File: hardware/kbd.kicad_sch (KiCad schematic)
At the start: 75 parts, among them J1 Conn_01x12_MountingPin, J2 Conn_01x12_MountingPin, SW00 SW_Push, SW01 SW_Push, SW02 SW_Push, SW03 SW_Push, SW04 SW_Push, SW05 SW_Push, SW10 SW_Push, SW11 SW_Push, SW12 SW_Push, SW13 SW_Push, SW14 SW_Push, SW15 SW_Push, SW20 SW_Push, SW21 SW_Push, SW22 SW_Push, SW23 SW_Push, SW24 SW_Push, SW25 SW_Push, SW30 SW_Push, SW31 SW_Push, SW32 SW_Push, SW33 SW_Push, SW34 SW_Push, SW35 SW_Push, SW36 SW_Push, SW37 SW_Push, U1 CH582, U2 74HC165, U4 74HC165

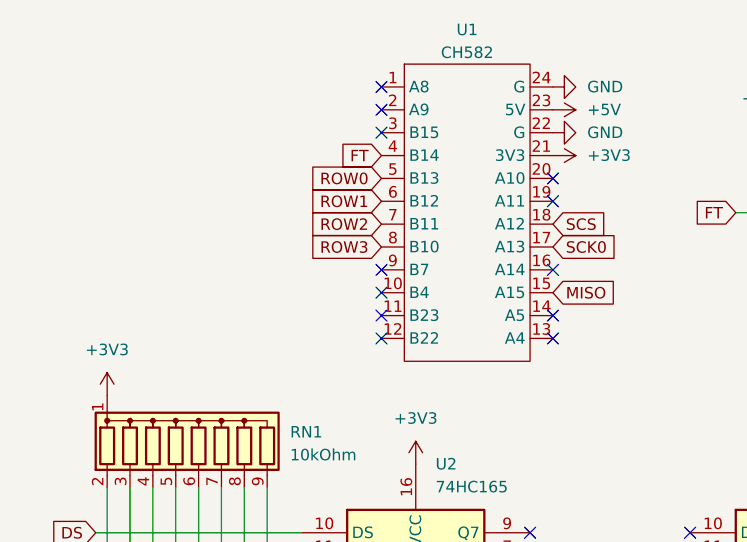
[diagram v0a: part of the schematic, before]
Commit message: Fixed row2 and row3 pin connections and added gerber files
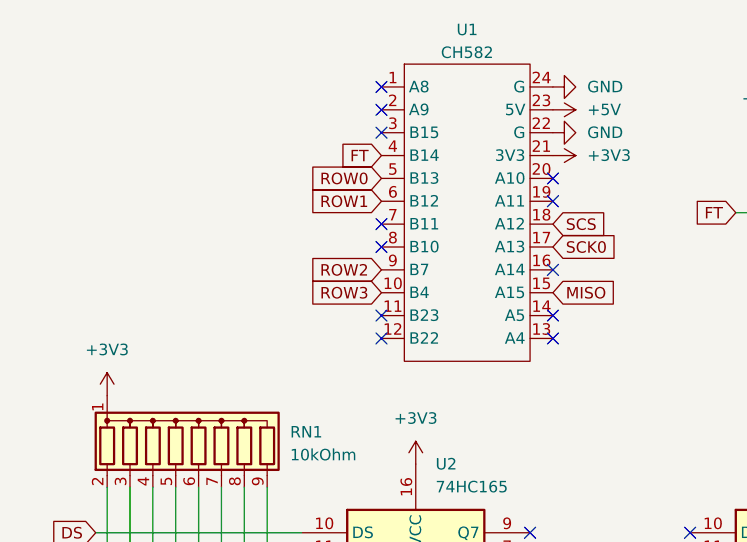
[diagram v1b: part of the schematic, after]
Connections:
- net ROW2: now also U1.9 (B7); no longer U1.7 (B11)
- net ROW3: now also U1.10 (B4); no longer U1.8 (B10)

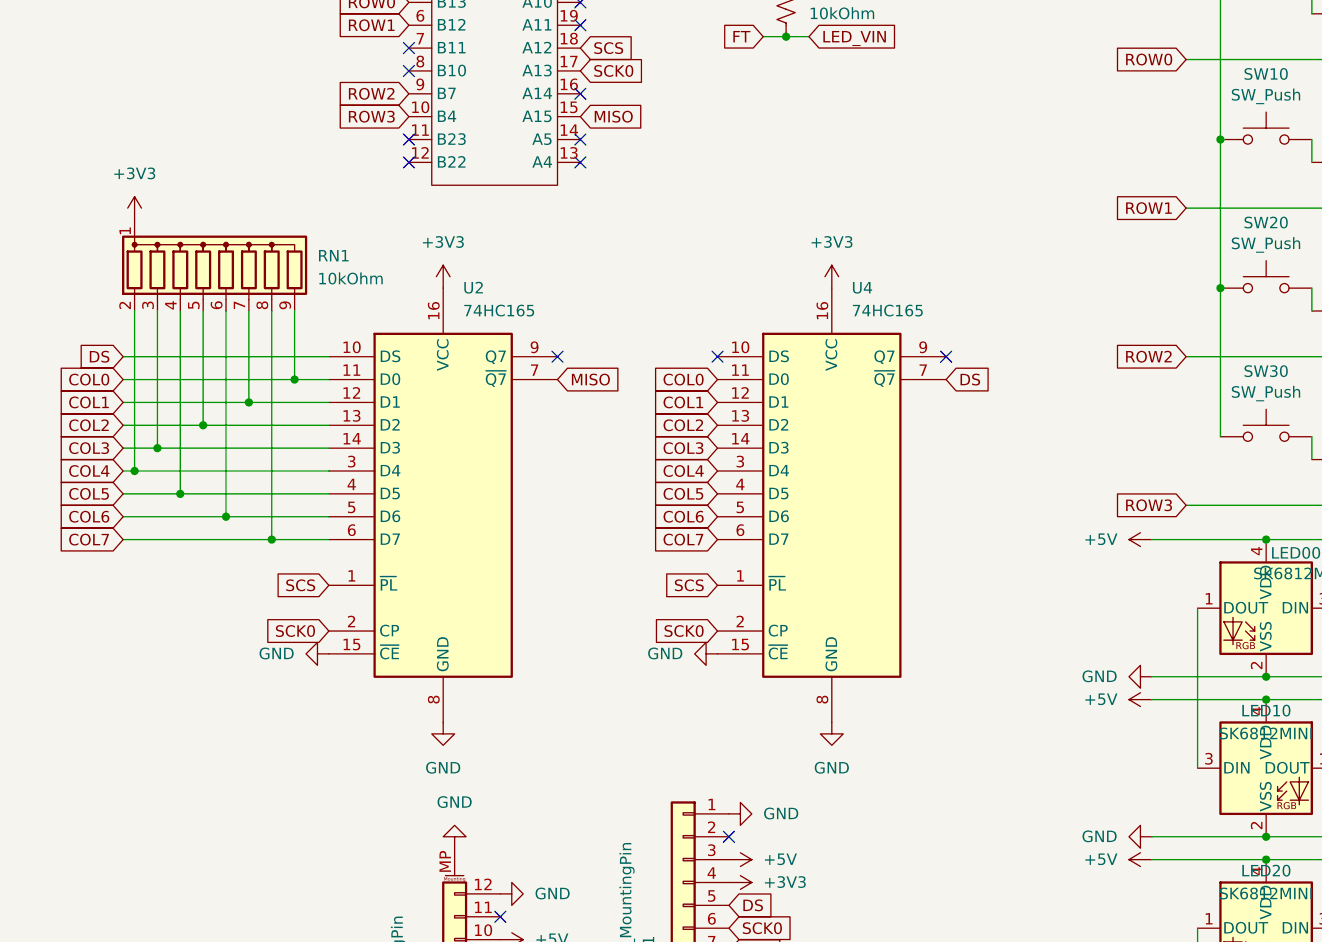
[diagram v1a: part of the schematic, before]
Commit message: Replaced SIP resistor with 0602x8
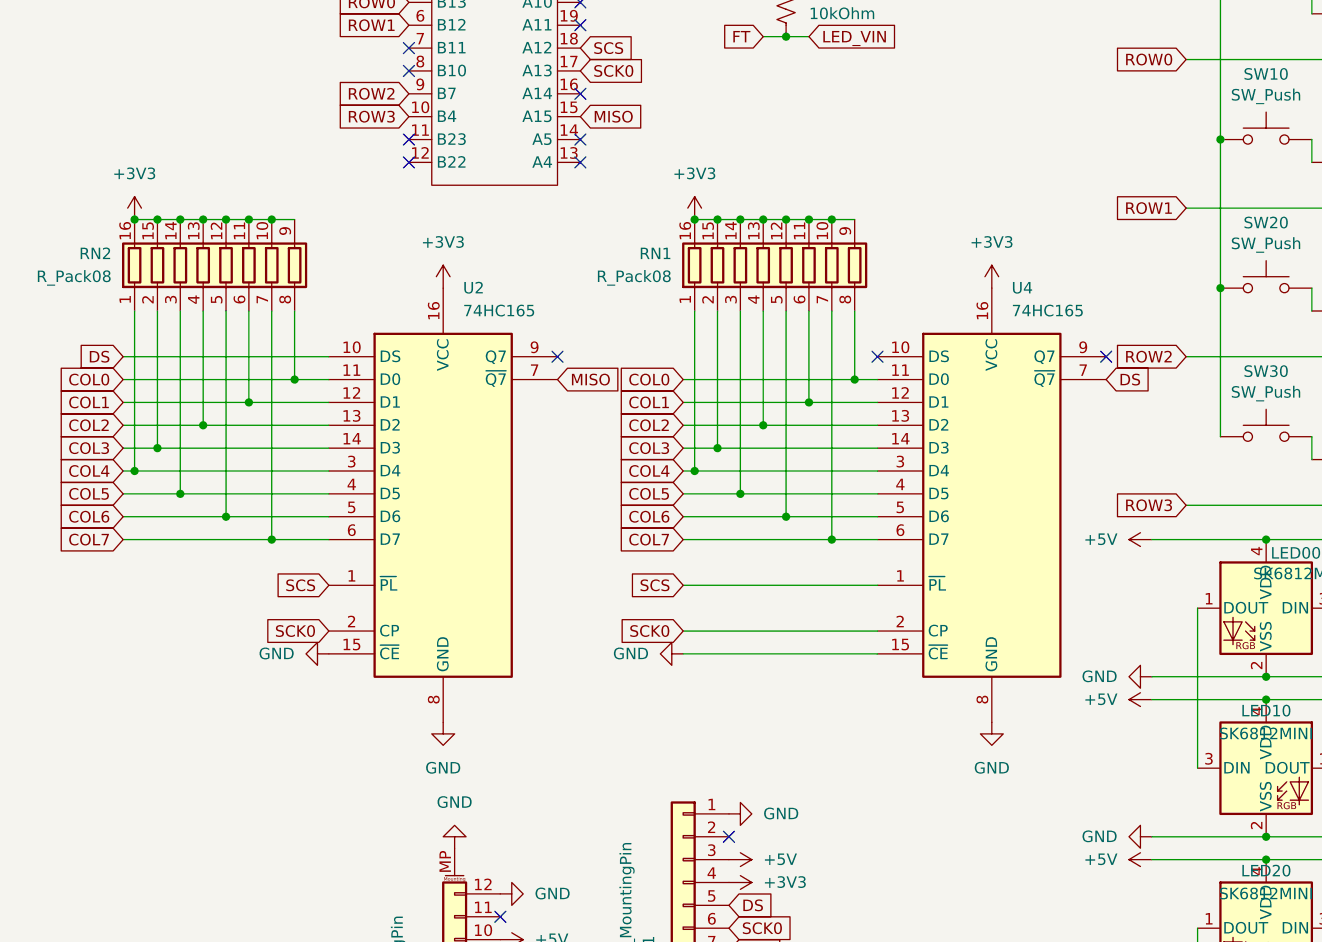
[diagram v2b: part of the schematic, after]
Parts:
- removed RN1: 10kOhm, Resistor_THT:R_Array_SIP9, symbol Device:R_Network08
- added RN1, RN2: R_Pack08, Resistor_SMD:R_Array_Convex_8x0602, symbol Device:R_Pack08
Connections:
- net +3V3: now also RN1.10 (R7.2), RN1.11 (R6.2), RN1.12 (R5.2), RN1.13 (R4.2), RN1.14 (R3.2), RN1.15 (R2.2), RN1.16 (R1.2), RN1.9 (R8.2), RN2.10 (R7.2), RN2.11 (R6.2), RN2.12 (R5.2), RN2.13 (R4.2), RN2.14 (R3.2), RN2.15 (R2.2), RN2.16 (R1.2), RN2.9 (R8.2)
- net COL0: now also RN1.8 (R8.1), RN2.8 (R8.1)
- net COL1: now also RN1.6 (R6.1), RN2.6 (R6.1)
- net COL2: now also RN1.4 (R4.1), RN2.4 (R4.1)
- net COL3: now also RN1.2 (R2.1), RN2.2 (R2.1)
- net COL4: now also RN1.1 (R1.1), RN2.1 (R1.1)
- net COL5: now also RN1.3 (R3.1), RN2.3 (R3.1)
- net COL6: now also RN1.5 (R5.1), RN2.5 (R5.1)
- net COL7: now also RN1.7 (R7.1), RN2.7 (R7.1)
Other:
- moved on the sheet: U4
